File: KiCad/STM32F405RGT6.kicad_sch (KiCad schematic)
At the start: 44 parts, among them J1 Conn_02x05_Odd_Even, J2 USB_C_Receptacle_USB2.0, SW1 TS-1187A, SW2 TS-1187A, U1 AMS1117-3.3, U2 M24C02-RMN, U3 STM32F405RGTx, U4 SRV05-4, Y1 16MHz

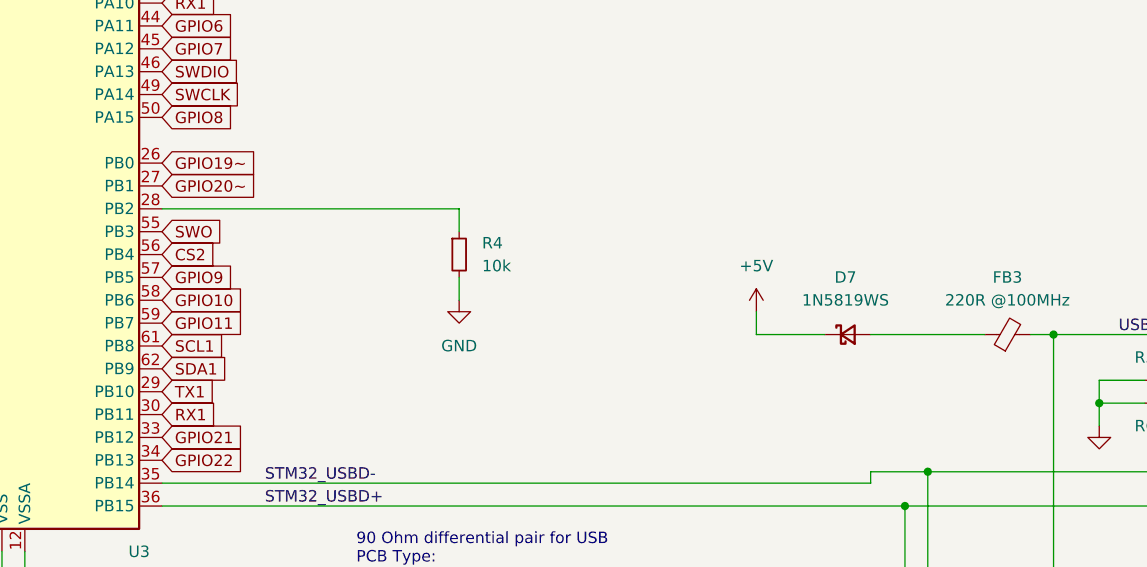
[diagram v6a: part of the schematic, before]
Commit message: added USB 3D model and PTC fuse
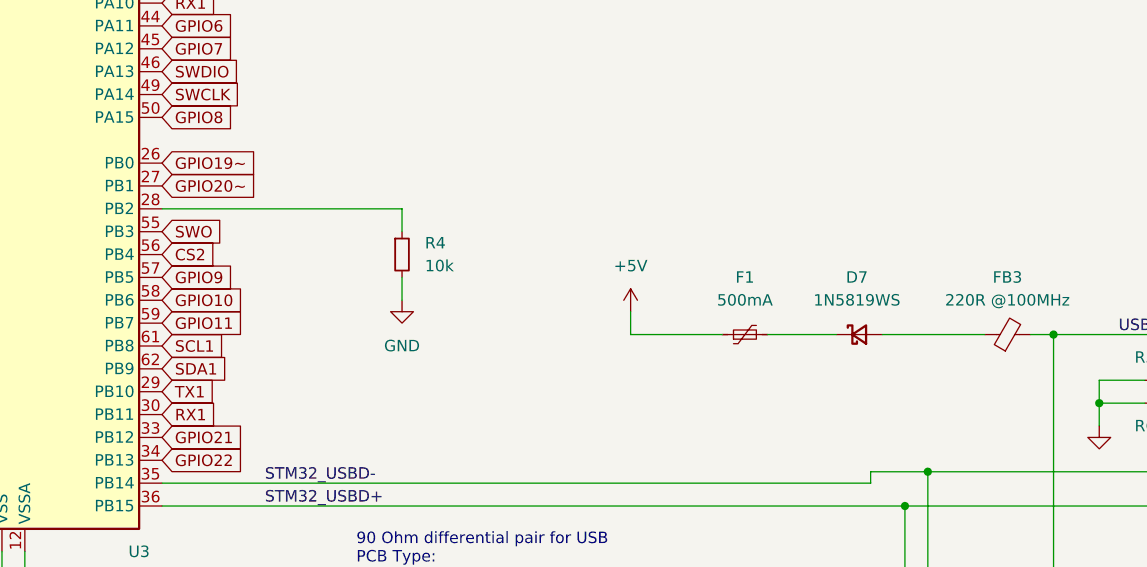
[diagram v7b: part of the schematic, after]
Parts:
- added F1: 500mA, Fuse:Fuse_1206_3216Metric, symbol Device:Polyfuse_Small
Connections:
- net +5V: now also F1.1; no longer D7.1 (K)
- new net: D7.1 (K), F1.2
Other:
- moved on the sheet: D7, R4

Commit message: Updated Schematic and PCB
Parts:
- removed C4: 100nF, Capacitor_SMD:C_0603_1608Metric, symbol Device:C_Small
- removed JP2: EXT +3V3A, Connector_PinHeader_2.54mm:PinHeader_1x02_P2.54mm_Vertical, symbol Jumper:Jumper_2_Open
- removed SW2: TS-1187A, Button_Switch_SMD:SW_SPST_SKQG_WithStem, symbol Switch:SW_SPST
- added C1, C6: 100nF, Capacitor_SMD:C_0603_1608Metric, symbol Device:C_Small
- added D8: LED_Small, LED_SMD:LED_0603_1608Metric, symbol Device:LED_Small
- added JP2: EXT +3V3A, Jumper:SolderJumper-3_P1.3mm_Bridged12_RoundedPad1.0x1.5mm, symbol Jumper:SolderJumper_3_Bridged12
- added R1, R3: 10k, Resistor_SMD:R_0603_1608Metric, symbol Device:R_Small
- added R11: 1k, Resistor_SMD:R_0603_1608Metric, symbol Device:R_Small
- added R4, R5: 5k1, Resistor_SMD:R_0603_1608Metric, symbol Device:R_Small
- added SW1: TS-1187A, Button_Switch_SMD:SW_SPST_SKQG_WithStem, symbol Switch:SW_SPST
- renumbered C1 to C17, C2 to C18, C3 to C2, C5 to C3, C6 to C4, C7 to C5, C8 to C7, C9 to C8, C17 to C9, D4 to D1, D5 to D2, D6 to D3, D2 to D4, D3 to D5, D7 to D6, D1 to D7, R6 to R10, R1 to R2, R2 to R6, R3 to R7, R4 to R8, R5 to R9, SW1 to SW2, U2 to U1, U3 to U2, U1 to U3
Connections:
- net TODO is gone; now on net GPIO19~: D3.4 (DIN)
- net +3.3VA: now also JP2.3 (B); no longer FB2.2
- net +3V3: now also U1.8 (VCC), C6.1, D8.2 (A), JP2.1 (A), R1.1, R3.1, R4.1, R5.1; no longer C2.1, SW2.2 (B), U2.7 (NRST)
- net GND: now also U1.4 (VSS), C1.2, C6.2, R11.2, SW1.1 (A)
- net GPIO20~: now also C1.1, R1.2, SW1.2 (B)
- net SCL1: now also R4.2
- net SDA1: now also R5.2
- new net: FB2.2, JP2.2 (C)
- new net: D8.1 (K), R11.1
- new net NRST_SW: C2.1, R3.2, SW2.2 (B), U2.7 (NRST)
- no-connect marks 6 -> 9
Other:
- note added: "USB +5V to +3V3"
- moved on the sheet: C17, C18, C2, C9, D1, D2, D3, D4, D5, D7, J1, R6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
